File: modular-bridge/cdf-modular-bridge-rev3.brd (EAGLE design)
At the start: 50.8 x 58.4 mm, 25 parts, among them Q1 Ixgh48n60a3, Q2 Ixgh48n60a3, T1 PULSE-P0584NL

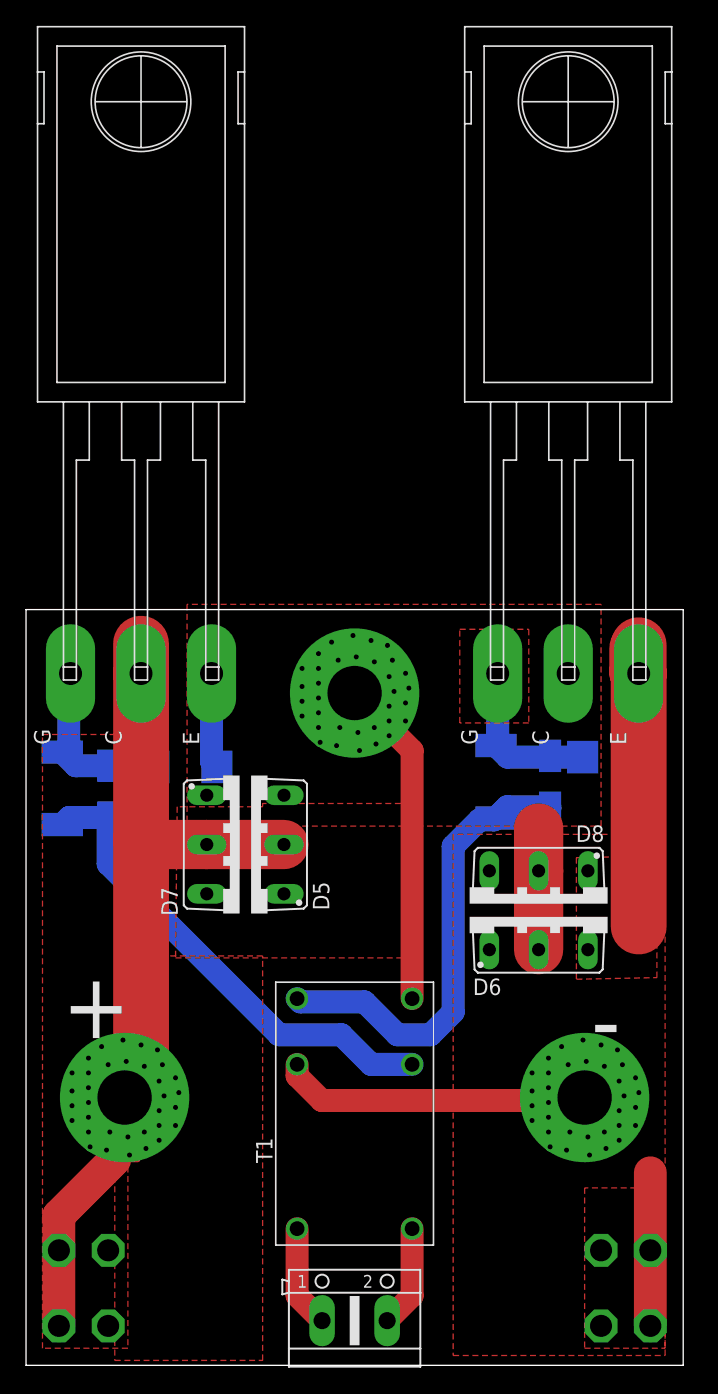
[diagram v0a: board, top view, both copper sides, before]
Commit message: add vias
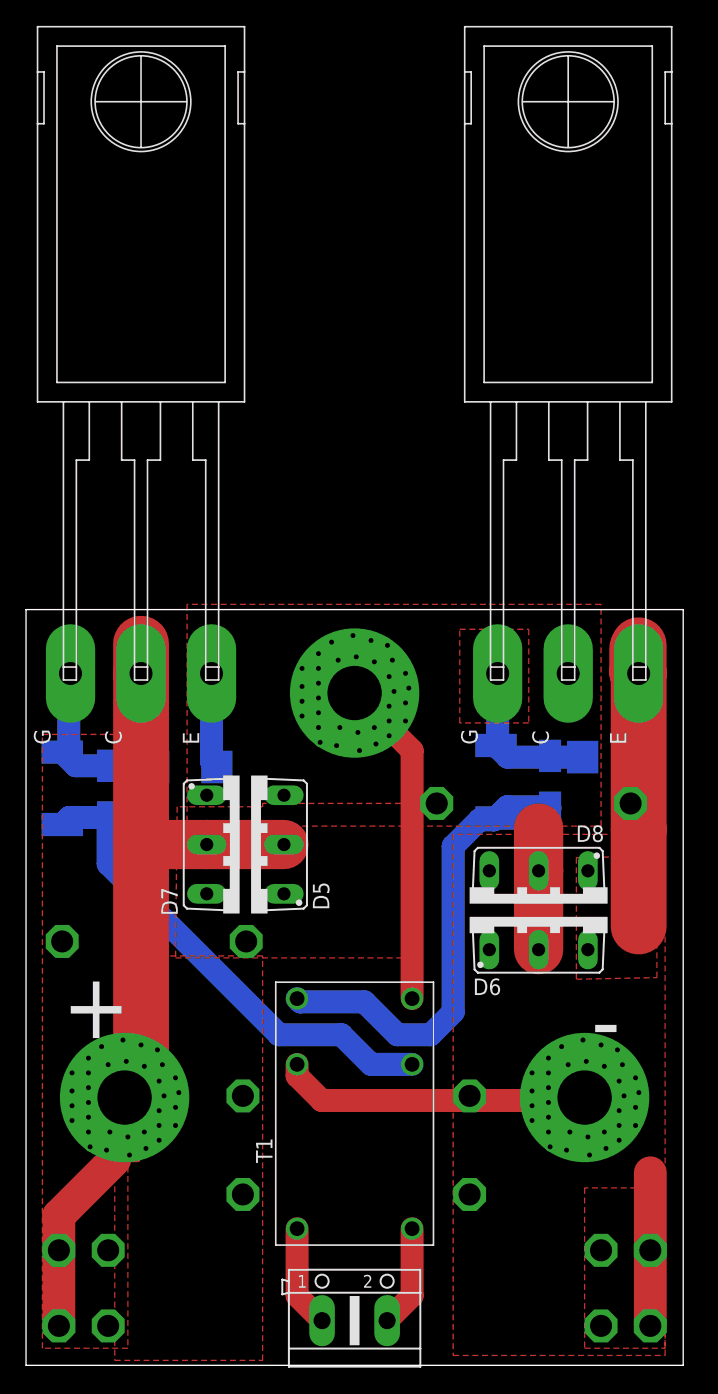
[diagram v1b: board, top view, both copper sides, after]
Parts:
- added TP10, TP11, TP12, TP13, TP14, TP15, TP16, TP9: PTR1PAD1-17, testpad:P1-17
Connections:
- net DC+: now also TP10.TP, TP11.TP, TP9.TP
- net DC-: now also TP14.TP, TP15.TP, TP16.TP
- net OUT: now also TP12.TP, TP13.TP
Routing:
- net DC-: track 66.2 -> 68.9 mm
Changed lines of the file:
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@@
 <attribute name="VALUE" x="48.26" y="8.89" size="0.0254" layer="27"/>
+</element>
+<element name="TP9" library="testpad" package="P1-17" value="PTR1PAD1-17" x="2.794" y="32.766" smashed="yes">
+<attribute name="TP_SIGNAL_NAME" value="" x="1.524" y="29.591" size="1" layer="37"/>
+<attribute name="VALUE" x="2.794" y="32.766" size="0.0254" layer="27"/>
+</element>
+<element name="TP10" library="testpad" package="P1-17" value="PTR1PAD1-17" x="16.764" y="20.828" smashed="yes">
+<attribute name="TP_SIGNAL_NAME" value="" x="15.494" y="17.653" size="1" layer="37"/>
+<attribute name="VALUE" x="16.764" y="20.828" size="0.0254" layer="27"/>
+</element>
+<element name="TP11" library="testpad" package="P1-17" value="PTR1PAD1-17" x="16.764" y="13.208" smashed="yes">
+<attribute name="TP_SIGNAL_NAME" value="" x="15.494" y="10.033" size="1" layer="37"/>
+<attribute name="VALUE" x="16.764" y="13.208" size="0.0254" layer="27"/>
+</element>
+<element name="TP14" library="testpad" package="P1-17" value="PTR1PAD1-17" x="34.29" y="20.828" smashed="yes">
+<attribute name="TP_SIGNAL_NAME" value="" x="33.02" y="17.653" size="1" layer="37"/>
+<attribute name="VALUE" x="34.29" y="20.828" size="0.0254" layer="27"/>
+</element>
+<element name="TP15" library="testpad" package="P1-17" value="PTR1PAD1-17" x="34.29" y="13.208" smashed="yes">
+<attribute name="TP_SIGNAL_NAME" value="" x="33.02" y="10.033" size="1" layer="37"/>
+<attribute name="VALUE" x="34.29" y="13.208" size="0.0254" layer="27"/>
+</element>
+<element name="TP16" library="testpad" package="P1-17" value="PTR1PAD1-17" x="46.736" y="43.434" smashed="yes">
+<attribute name="TP_SIGNAL_NAME" value="" x="45.466" y="40.259" size="1" layer="37"/>
+<attribute name="VALUE" x="46.736" y="43.434" size="0.0254" layer="27"/>
+</element>
+<element name="TP12" library="testpad" package="P1-17" value="PTR1PAD1-17" x="31.75" y="43.434" smashed="yes">
+<attribute name="TP_SIGNAL_NAME" value="" x="30.48" y="40.259" size="1" layer="37"/>
+<attribute name="VALUE" x="31.75" y="43.434" size="0.0254" layer="27"/>
+</element>
+<element name="TP13" library="testpad" package="P1-17" value="PTR1PAD1-17" x="17.018" y="32.766" smashed="yes">
+<attribute name="TP_SIGNAL_NAME" value="" x="15.748" y="29.591" size="1" layer="37"/>
+<attribute name="VALUE" x="17.018" y="32.766" size="0.0254" layer="27"/>
 </element>
 </elements>
@@
 <vertex x="18.288" y="43.18"/>
 </polygon>
+<contactref element="TP13" pad="TP"/>
+<contactref element="TP12" pad="TP"/>
 </signal>
 <signal name="N$5">
@@
 <contactref element="Q2" pad="E"/>
 <contactref element="DC-" pad="X"/>
-<wire x1="47.36" y1="33.9234" x2="47.36" y2="53.4784" width="4.318" layer="1"/>
+<wire x1="47.36" y1="33.9234" x2="47.36" y2="41.402" width="4.318" layer="1"/>
+<wire x1="47.36" y1="41.402" x2="47.36" y2="53.4784" width="4.318" layer="1"/>
 <wire x1="47.36" y1="53.4784" x2="47.36" y2="55.6624" width="4.318" layer="1"/>
 <wire x1="47.244" y1="55.3974" x2="47.244" y2="53.5944" width="4.318" layer="1"/>
@@
 <contactref element="TP7" pad="TP"/>
 <contactref element="TP8" pad="TP"/>
+<contactref element="TP16" pad="TP"/>
+<contactref element="TP15" pad="TP"/>
+<contactref element="TP14" pad="TP"/>
+<wire x1="46.736" y1="43.434" x2="47.36" y2="43.434" width="0.4064" layer="1"/>
+<wire x1="47.36" y1="43.434" x2="47.36" y2="41.402" width="0.4064" layer="1"/>
 </signal>
 <signal name="N$7">
@@
 <contactref element="TP6" pad="TP"/>
 <contactref element="TP5" pad="TP"/>
+<contactref element="TP9" pad="TP"/>
+<contactref element="TP10" pad="TP"/>
+<contactref element="TP11" pad="TP"/>
 </signal>
 <signal name="N$1">

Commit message: misc changes, rev4 of modular bridge
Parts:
- moved D3 3.81 mm to (12.3, 42.4)
- moved D4 3.81 mm to (45.5, 43.2)
- moved D5 3.81 mm to (17.4, 36.4)
- moved D7 3.81 mm to (16.5, 36.4)
- moved DC+ 3.81 mm to (7.62, 16.9)
- moved DC- 3.81 mm to (43.2, 16.9)
- moved OUT 3.81 mm to (25.4, 48.2)
- moved Q1 3.81 mm to (8.89, 93.9)
- moved Q2 3.81 mm to (41.9, 93.9)
- moved R1 3.81 mm to (2.79, 40.8)
- moved T1 3.81 mm to (25.4, 19.5), flipped to the bottom
- moved TP11 3.81 mm to (16.8, 9.40)
- moved TP15 3.81 mm to (34.3, 9.40)
- moved D6 3.81 mm to (39.6, 30.9)
- moved D8 3.81 mm to (39.6, 31.9)
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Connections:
- net N$1: now also X1.2; no longer X1.1
- net N$2: now also X1.1; no longer X1.2
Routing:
- net DC-: track 68.9 -> 48.0 mm
- net OUT: track 42.8 -> 27.7 mm
- net N$7: track 35.6 -> 21.9 mm
- net N$8: track 37.3 -> 28.9 mm
- net N$1: track 7.91 -> 4.10 mm
- net N$2: track 7.91 -> 4.10 mm
- net DC+: track 59.4 -> 55.6 mm
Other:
- board size 50.8 x 58.4 mm -> 50.8 x 54.6 mm
